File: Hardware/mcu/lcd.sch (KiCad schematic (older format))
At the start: 19 parts, among them P801 JP_SPI, P802 JP_SPI2, Q1001 NPN, U1001 MI0283QT-2, U1002 AD7843

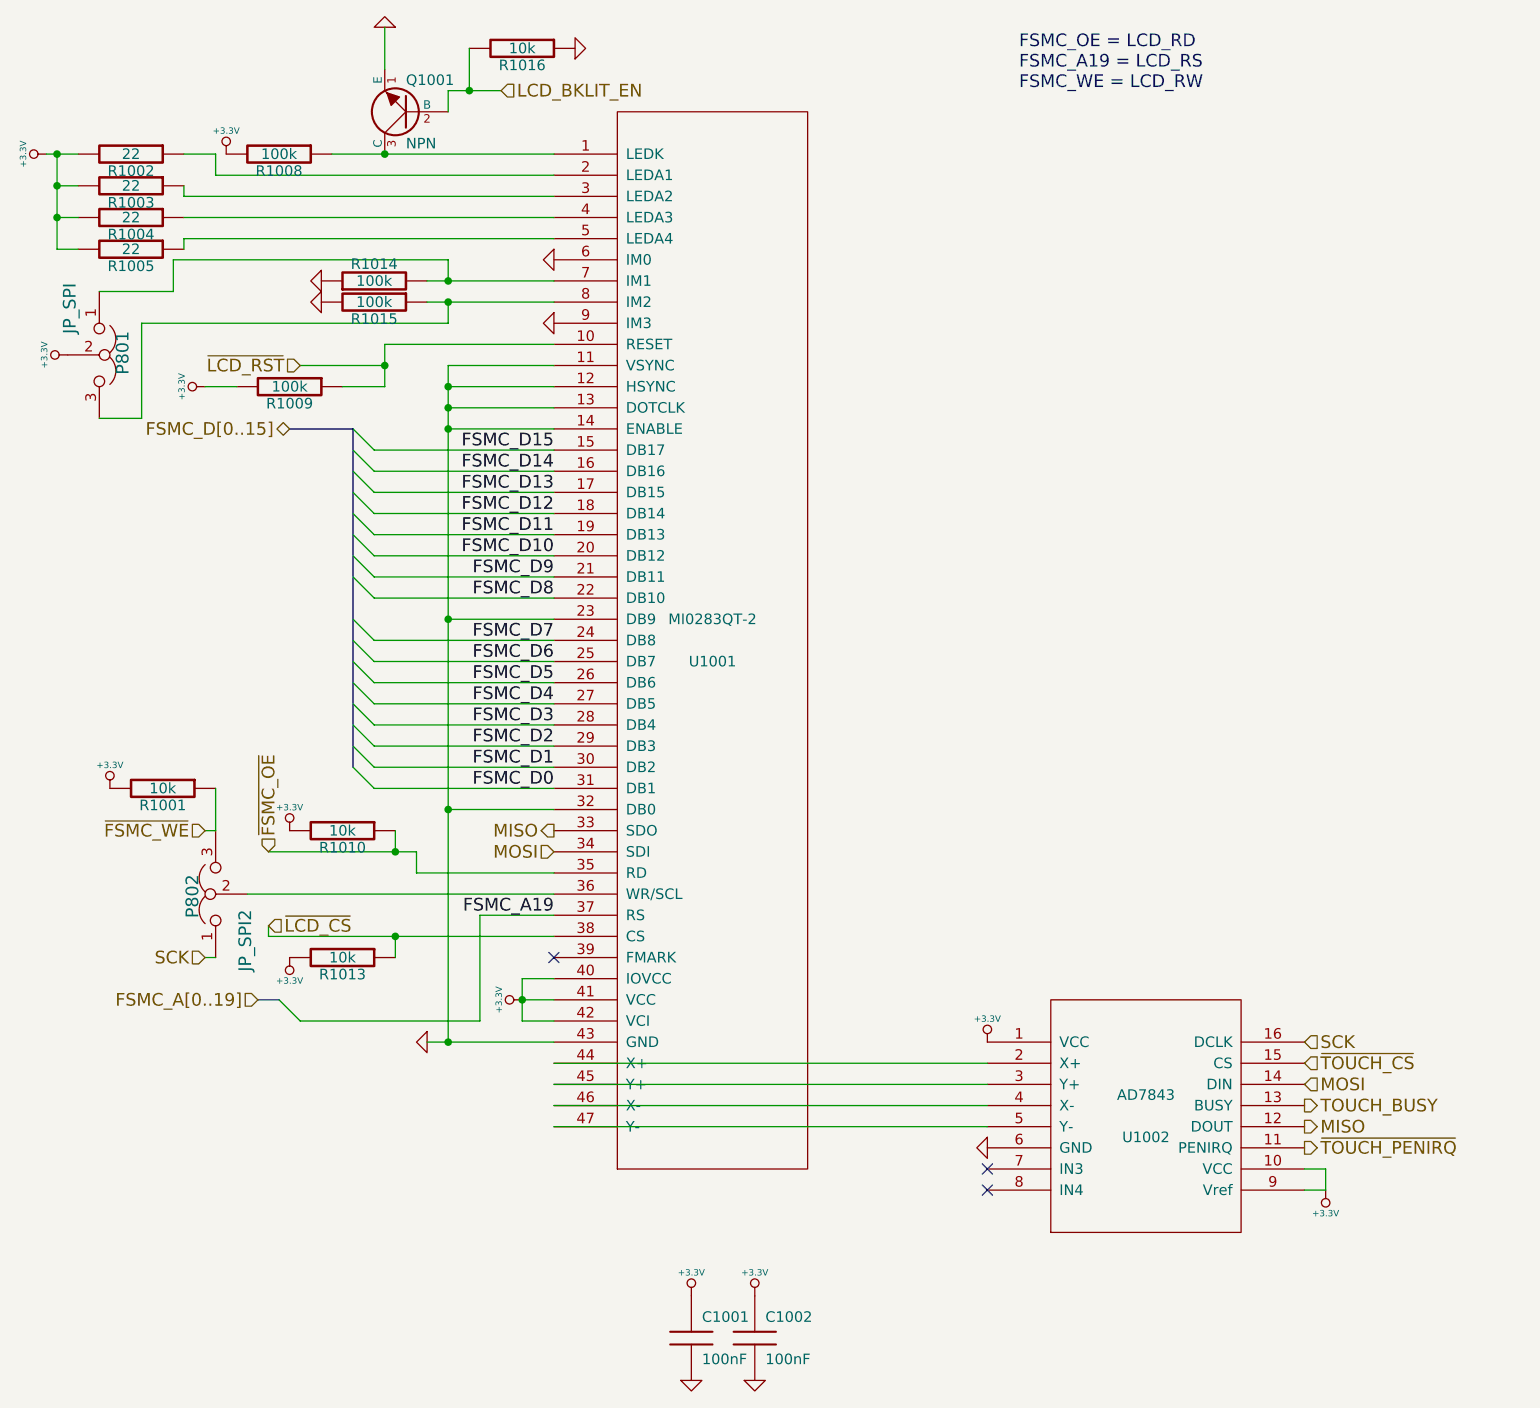
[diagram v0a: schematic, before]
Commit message: changes to mcu, new format and using a display adapter board
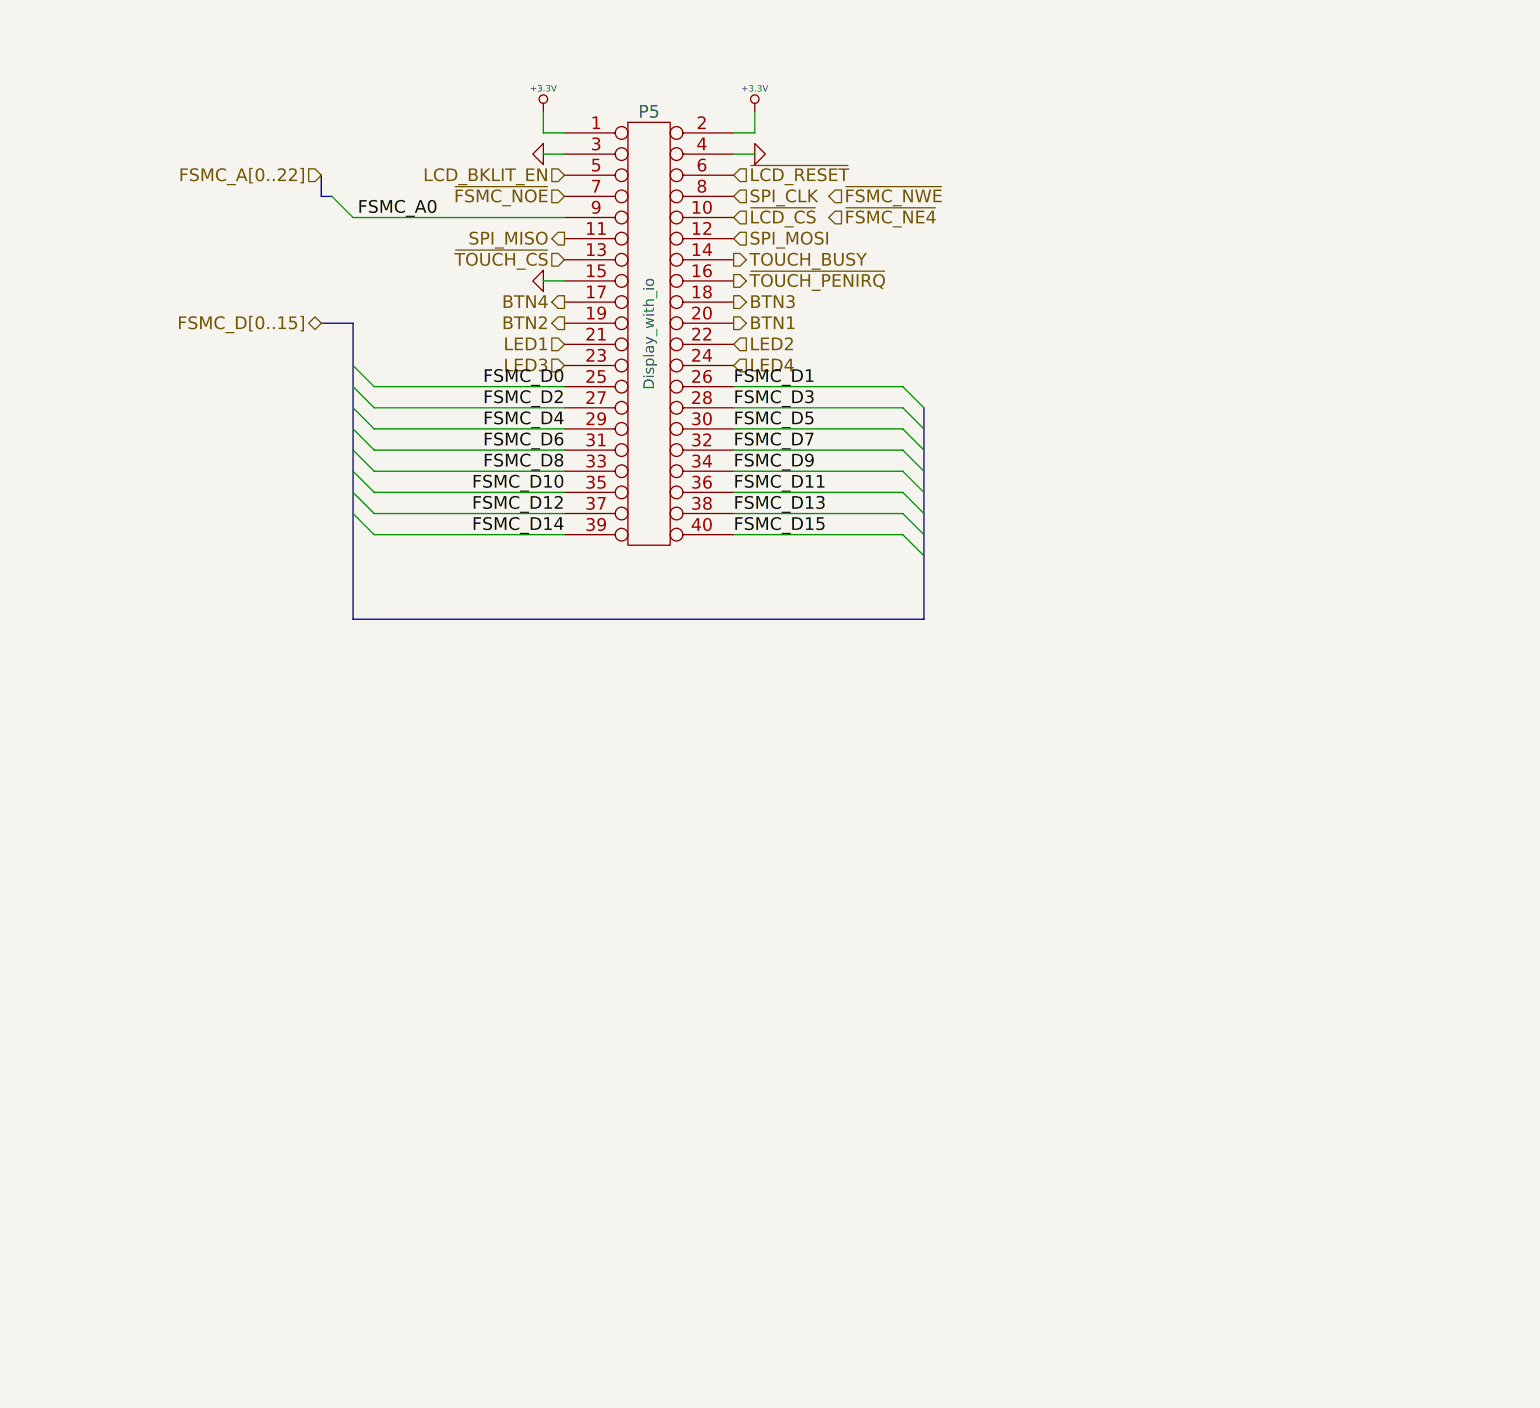
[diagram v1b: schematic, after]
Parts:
- removed C1001, C1002: 100nF, symbol C
- removed P801: JP_SPI, symbol JUMPER3
- removed P802: JP_SPI2, symbol JUMPER3
- removed Q1001: NPN, symbol NPN
- removed R1001, R1010, R1013, R1016: 10k, symbol R
- removed R1002, R1003, R1004, R1005: 22, symbol R
- removed R1008, R1009, R1014, R1015: 100k, symbol R
- removed U1001: MI0283QT-2, symbol MI0283QT-2
- removed U1002: AD7843, symbol AD7843
- added P5: Display_with_io, symbol CONN_20X2
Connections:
- net +3.3V: now also P5.1 (P1), P5.2 (P2)
- net FSMC_D0: now also P5.25
- net FSMC_D1: now also P5.26 (P26)
- net FSMC_D10: now also P5.35 (P35)
- net FSMC_D11: now also P5.36 (P36)
- net FSMC_D12: now also P5.37 (P37)
- net FSMC_D13: now also P5.38 (P38)
- net FSMC_D14: now also P5.39 (P39)
- net FSMC_D15: now also P5.40 (P40)
- net FSMC_D2: now also P5.27 (P27)
- net FSMC_D3: now also P5.28 (P28)
- net FSMC_D4: now also P5.29 (P29)
- net FSMC_D5: now also P5.30 (P30)
- net FSMC_D6: now also P5.31 (P31)
- net FSMC_D7: now also P5.32 (P32)
- net FSMC_D8: now also P5.33 (P33)
- net FSMC_D9: now also P5.34 (P34)
- net GND: now also P5.15 (P15), P5.3 (P3), P5.4 (P4)
- net LCD_BKLIT_EN: now also P5.5 (P5)
- net TOUCH_BUSY: now also P5.14 (P14)
- net ~LCD_CS: now also P5.10 (P10)
- net ~TOUCH_CS: now also P5.13 (P13)
- net ~TOUCH_PENIRQ: now also P5.16 (P16)
- new net BTN1: P5.20 (P20)
- new net BTN2: P5.19 (P19)
- new net BTN3: P5.18 (P18)
- new net BTN4: P5.17 (P17)
- new net FSMC_A0: P5.9 (P9)
- new net LED1: P5.21 (P21)
- new net LED2: P5.22 (P22)
- new net LED3: P5.23 (P23)
- new net LED4: P5.24 (P24)
- new net SPI_CLK: P5.8 (P8)
- new net SPI_MISO: P5.11 (P11)
- new net SPI_MOSI: P5.12 (P12)
- new net ~FSMC_NOE: P5.7 (P7)
- new net ~LCD_RESET: P5.6 (P6)
- no-connect marks 3 -> 0
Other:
- note removed: "FSMC_OE = LCD_RD\nFSMC_A19 = LCD_RS\nFSMC_WE = LCD_RW"
